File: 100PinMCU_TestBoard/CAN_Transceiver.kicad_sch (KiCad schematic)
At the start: 9 parts, among them IC1 TCAN3413DR

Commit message: pre japan flight
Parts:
- renumbered C1 to C2, C2 to C3, C3 to C4, C4 to C5, D6 to D8, JP11 to JP7, R9 to R11, R10 to R12
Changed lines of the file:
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@@
 		(on_board yes)
 		(dnp no)
-		(property "Reference" "C2"
+		(property "Reference" "C3"
 			(at 76.2 73.66 0)
 			(effects
@@
 			(project "100PinMCU_ESP32_TestBoard"
 				(path "/abcdaa41-14f3-4587-9aac-314b09095246/7ebae12d-faed-4676-bea3-8e8b5526eaae"
-					(reference "C12")
+					(reference "C13")
 					(unit 1)
 				)
 				(path "/abcdaa41-14f3-4587-9aac-314b09095246/cbcec814-e1b6-4f49-9afe-3e964e4b41da"
-					(reference "C2")
+					(reference "C3")
 					(unit 1)
 				)
@@
 		(on_board yes)
 		(dnp no)
-		(property "Reference" "C4"
+		(property "Reference" "C5"
 			(at 194.564 88.646 0)
 			(effects
@@
 			(project "100PinMCU_ESP32_TestBoard"
 				(path "/abcdaa41-14f3-4587-9aac-314b09095246/7ebae12d-faed-4676-bea3-8e8b5526eaae"
-					(reference "C14")
+					(reference "C15")
 					(unit 1)
 				)
 				(path "/abcdaa41-14f3-4587-9aac-314b09095246/cbcec814-e1b6-4f49-9afe-3e964e4b41da"
-					(reference "C4")
+					(reference "C5")
 					(unit 1)
 				)
@@
 		(dnp no)
 		(fields_autoplaced yes)
-		(property "Reference" "JP11"
+		(property "Reference" "JP7"
 			(at 215.9 78.74 0)
 			(effects
@@
 			(project "100PinMCU_ESP32_TestBoard"
 				(path "/abcdaa41-14f3-4587-9aac-314b09095246/7ebae12d-faed-4676-bea3-8e8b5526eaae"
-					(reference "JP12")
+					(reference "JP8")
 					(unit 1)
 				)
 				(path "/abcdaa41-14f3-4587-9aac-314b09095246/cbcec814-e1b6-4f49-9afe-3e964e4b41da"
-					(reference "JP11")
+					(reference "JP7")
 					(unit 1)
 				)
@@
 		(on_board yes)
 		(dnp no)
-		(property "Reference" "C3"
+		(property "Reference" "C4"
 			(at 88.138 73.66 0)
 			(effects
@@
 			(project "100PinMCU_ESP32_TestBoard"
 				(path "/abcdaa41-14f3-4587-9aac-314b09095246/7ebae12d-faed-4676-bea3-8e8b5526eaae"
-					(reference "C13")
+					(reference "C14")
 					(unit 1)
 				)
 				(path "/abcdaa41-14f3-4587-9aac-314b09095246/cbcec814-e1b6-4f49-9afe-3e964e4b41da"
-					(reference "C3")
+					(reference "C4")
 					(unit 1)
 				)
@@
 		(on_board yes)
 		(dnp no)
-		(property "Reference" "C1"
+		(property "Reference" "C2"
 			(at 65.278 73.66 0)
 			(effects
@@
 			(project "100PinMCU_ESP32_TestBoard"
 				(path "/abcdaa41-14f3-4587-9aac-314b09095246/7ebae12d-faed-4676-bea3-8e8b5526eaae"
-					(reference "C11")
+					(reference "C12")
 					(unit 1)
 				)
 				(path "/abcdaa41-14f3-4587-9aac-314b09095246/cbcec814-e1b6-4f49-9afe-3e964e4b41da"
-					(reference "C1")
+					(reference "C2")
 					(unit 1)
 				)
@@
 		(on_board yes)
 		(dnp no)
-		(property "Reference" "R10"
+		(property "Reference" "R12"
 			(at 201.93 80.01 90)
 			(effects
@@
 			(project "100PinMCU_ESP32_TestBoard"
 				(path "/abcdaa41-14f3-4587-9aac-314b09095246/7ebae12d-faed-4676-bea3-8e8b5526eaae"
-					(reference "R20")
+					(reference "R22")
 					(unit 1)
 				)
 				(path "/abcdaa41-14f3-4587-9aac-314b09095246/cbcec814-e1b6-4f49-9afe-3e964e4b41da"
-					(reference "R10")
+					(reference "R12")
 					(unit 1)
 				)
@@
 		(dnp no)
 		(fields_autoplaced yes)
-		(property "Reference" "D6"
+		(property "Reference" "D8"
 			(at 196.85 46.99 0)
 			(effects
@@
 			(project "100PinMCU_ESP32_TestBoard"
 				(path "/abcdaa41-14f3-4587-9aac-314b09095246/7ebae12d-faed-4676-bea3-8e8b5526eaae"
-					(reference "D13")
+					(reference "D15")
 					(unit 1)
 				)
 				(path "/abcdaa41-14f3-4587-9aac-314b09095246/cbcec814-e1b6-4f49-9afe-3e964e4b41da"
-					(reference "D6")
+					(reference "D8")
 					(unit 1)
 				)
@@
 		(on_board yes)
 		(dnp no)
-		(property "Reference" "R9"
+		(property "Reference" "R11"
 			(at 176.53 80.01 90)
 			(effects
@@
 			(project "100PinMCU_ESP32_TestBoard"
 				(path "/abcdaa41-14f3-4587-9aac-314b09095246/7ebae12d-faed-4676-bea3-8e8b5526eaae"
-					(reference "R19")
+					(reference "R21")
 					(unit 1)
 				)
 				(path "/abcdaa41-14f3-4587-9aac-314b09095246/cbcec814-e1b6-4f49-9afe-3e964e4b41da"
-					(reference "R9")
-					(unit 1)
-				)
+					(reference "R11")
+					(unit 1)
+				)

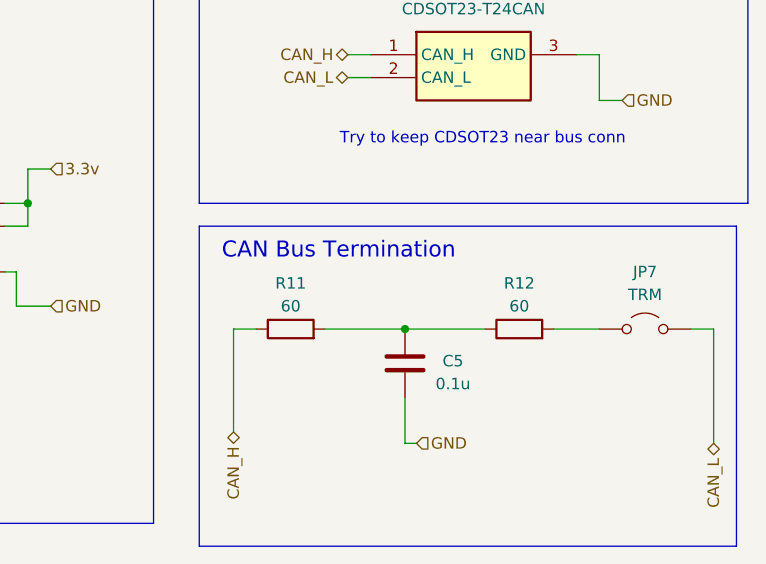
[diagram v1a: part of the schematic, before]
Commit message: add mux
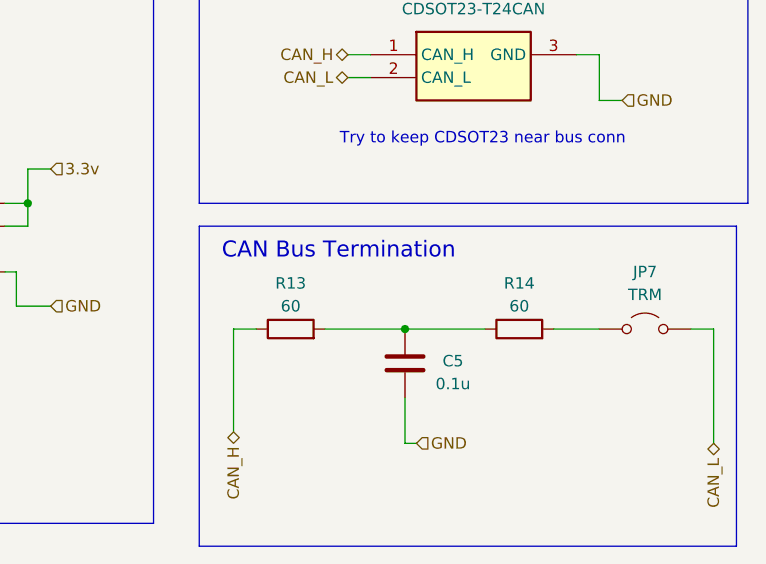
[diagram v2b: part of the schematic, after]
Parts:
- renumbered R11 to R13, R12 to R14
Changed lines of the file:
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@@
 		(on_board yes)
 		(dnp no)
-		(property "Reference" "R12"
+		(property "Reference" "R14"
 			(at 201.93 80.01 90)
 			(effects
@@
 			(project "100PinMCU_ESP32_TestBoard"
 				(path "/abcdaa41-14f3-4587-9aac-314b09095246/7ebae12d-faed-4676-bea3-8e8b5526eaae"
-					(reference "R22")
+					(reference "R24")
 					(unit 1)
 				)
 				(path "/abcdaa41-14f3-4587-9aac-314b09095246/cbcec814-e1b6-4f49-9afe-3e964e4b41da"
-					(reference "R12")
+					(reference "R14")
 					(unit 1)
 				)
@@
 		(on_board yes)
 		(dnp no)
-		(property "Reference" "R11"
+		(property "Reference" "R13"
 			(at 176.53 80.01 90)
 			(effects
@@
 			(project "100PinMCU_ESP32_TestBoard"
 				(path "/abcdaa41-14f3-4587-9aac-314b09095246/7ebae12d-faed-4676-bea3-8e8b5526eaae"
-					(reference "R21")
+					(reference "R23")
 					(unit 1)
 				)
 				(path "/abcdaa41-14f3-4587-9aac-314b09095246/cbcec814-e1b6-4f49-9afe-3e964e4b41da"
-					(reference "R11")
-					(unit 1)
-				)
+					(reference "R13")
+					(unit 1)
+				)

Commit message: erc
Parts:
- renumbered C2 to C5, C3 to C6, C4 to C7, C5 to C8, D8 to D11, JP7 to JP8, R13 to R19, R14 to R20
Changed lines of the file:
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@@
 		(on_board yes)
 		(dnp no)
-		(property "Reference" "C3"
+		(property "Reference" "C6"
 			(at 76.2 73.66 0)
 			(effects
@@
 			(project "100PinMCU_ESP32_TestBoard"
 				(path "/abcdaa41-14f3-4587-9aac-314b09095246/0e3bffe1-e2aa-4b27-b0c7-28d8996d7add"
-					(reference "C9")
+					(reference "C12")
 					(unit 1)
 				)
 				(path "/abcdaa41-14f3-4587-9aac-314b09095246/cbcec814-e1b6-4f49-9afe-3e964e4b41da"
-					(reference "C3")
+					(reference "C6")
 					(unit 1)
 				)
@@
 		(on_board yes)
 		(dnp no)
-		(property "Reference" "C5"
+		(property "Reference" "C8"
 			(at 194.564 88.646 0)
 			(effects
@@
 			(project "100PinMCU_ESP32_TestBoard"
 				(path "/abcdaa41-14f3-4587-9aac-314b09095246/0e3bffe1-e2aa-4b27-b0c7-28d8996d7add"
-					(reference "C11")
+					(reference "C14")
 					(unit 1)
 				)
 				(path "/abcdaa41-14f3-4587-9aac-314b09095246/cbcec814-e1b6-4f49-9afe-3e964e4b41da"
-					(reference "C5")
+					(reference "C8")
 					(unit 1)
 				)
@@
 		(dnp no)
 		(fields_autoplaced yes)
-		(property "Reference" "JP7"
+		(property "Reference" "JP8"
 			(at 215.9 78.74 0)
 			(effects
@@
 			(project "100PinMCU_ESP32_TestBoard"
 				(path "/abcdaa41-14f3-4587-9aac-314b09095246/0e3bffe1-e2aa-4b27-b0c7-28d8996d7add"
-					(reference "JP5")
+					(reference "JP9")
 					(unit 1)
 				)
 				(path "/abcdaa41-14f3-4587-9aac-314b09095246/cbcec814-e1b6-4f49-9afe-3e964e4b41da"
-					(reference "JP7")
+					(reference "JP8")
 					(unit 1)
 				)
@@
 		(on_board yes)
 		(dnp no)
-		(property "Reference" "C4"
+		(property "Reference" "C7"
 			(at 88.138 73.66 0)
 			(effects
@@
 			(project "100PinMCU_ESP32_TestBoard"
 				(path "/abcdaa41-14f3-4587-9aac-314b09095246/0e3bffe1-e2aa-4b27-b0c7-28d8996d7add"
-					(reference "C10")
+					(reference "C13")
 					(unit 1)
 				)
 				(path "/abcdaa41-14f3-4587-9aac-314b09095246/cbcec814-e1b6-4f49-9afe-3e964e4b41da"
-					(reference "C4")
+					(reference "C7")
 					(unit 1)
 				)
@@
 		(on_board yes)
 		(dnp no)
-		(property "Reference" "C2"
+		(property "Reference" "C5"
 			(at 65.278 73.66 0)
 			(effects
@@
 			(project "100PinMCU_ESP32_TestBoard"
 				(path "/abcdaa41-14f3-4587-9aac-314b09095246/0e3bffe1-e2aa-4b27-b0c7-28d8996d7add"
-					(reference "C8")
+					(reference "C11")
 					(unit 1)
 				)
 				(path "/abcdaa41-14f3-4587-9aac-314b09095246/cbcec814-e1b6-4f49-9afe-3e964e4b41da"
-					(reference "C2")
+					(reference "C5")
 					(unit 1)
 				)
@@
 		(on_board yes)
 		(dnp no)
-		(property "Reference" "R14"
+		(property "Reference" "R20"
 			(at 201.93 80.01 90)
 			(effects
@@
 			(project "100PinMCU_ESP32_TestBoard"
 				(path "/abcdaa41-14f3-4587-9aac-314b09095246/0e3bffe1-e2aa-4b27-b0c7-28d8996d7add"
-					(reference "R17")
+					(reference "R22")
 					(unit 1)
 				)
 				(path "/abcdaa41-14f3-4587-9aac-314b09095246/cbcec814-e1b6-4f49-9afe-3e964e4b41da"
-					(reference "R14")
+					(reference "R20")
 					(unit 1)
 				)
@@
 		(dnp no)
 		(fields_autoplaced yes)
-		(property "Reference" "D8"
+		(property "Reference" "D11"
 			(at 196.85 46.99 0)
 			(effects
@@
 			(project "100PinMCU_ESP32_TestBoard"
 				(path "/abcdaa41-14f3-4587-9aac-314b09095246/0e3bffe1-e2aa-4b27-b0c7-28d8996d7add"
-					(reference "D10")
+					(reference "D13")
 					(unit 1)
 				)
 				(path "/abcdaa41-14f3-4587-9aac-314b09095246/cbcec814-e1b6-4f49-9afe-3e964e4b41da"
-					(reference "D8")
+					(reference "D11")
 					(unit 1)
 				)
@@
 		(on_board yes)
 		(dnp no)
-		(property "Reference" "R13"
+		(property "Reference" "R19"
 			(at 176.53 80.01 90)
 			(effects
@@
 			(project "100PinMCU_ESP32_TestBoard"
 				(path "/abcdaa41-14f3-4587-9aac-314b09095246/0e3bffe1-e2aa-4b27-b0c7-28d8996d7add"
-					(reference "R2")
+					(reference "R21")
 					(unit 1)
 				)
 				(path "/abcdaa41-14f3-4587-9aac-314b09095246/cbcec814-e1b6-4f49-9afe-3e964e4b41da"
-					(reference "R13")
-					(unit 1)
-				)
+					(reference "R19")
+					(unit 1)
+				)
